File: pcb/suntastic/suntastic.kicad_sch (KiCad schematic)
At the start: 0 parts

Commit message: Rename sheet
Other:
- sheet UVLO with latched output: file uvlo_and latch.kicad_sch -> uvlo_and_latch.kicad_sch
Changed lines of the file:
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@@
       (effects (font (size 1.27 1.27)) (justify left bottom))
     )
-    (property "Sheetfile" "uvlo_and latch.kicad_sch" (at 167.64 65.3546 0) (show_name)
+    (property "Sheetfile" "uvlo_and_latch.kicad_sch" (at 167.64 65.3546 0) (show_name)
       (effects (font (size 1.27 1.27)) (justify left top))
     )

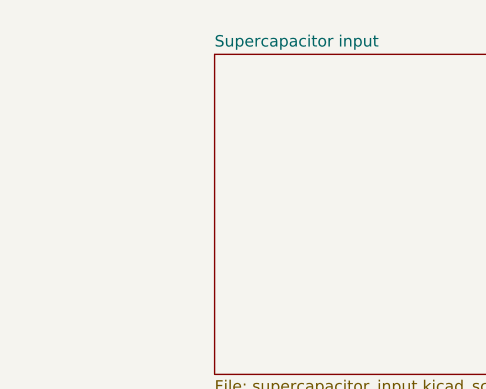
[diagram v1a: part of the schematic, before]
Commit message: Add load switch and RAK connector
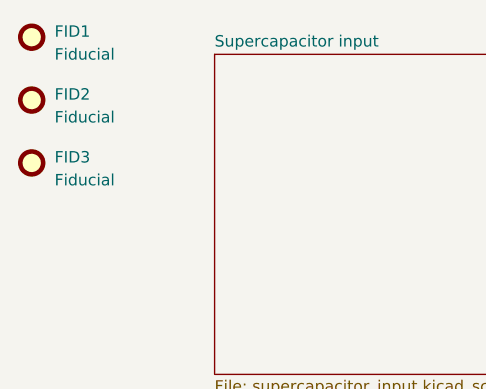
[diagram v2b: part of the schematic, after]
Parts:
- added FID1, FID2, FID3: Fiducial, Fiducial:Fiducial_1mm_Mask3mm, symbol Mechanical:Fiducial
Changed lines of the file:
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@@
     (comment 1 "An ultra low-power management board for meshtastic solar repeater devices.  ")
+  )
+  (symbol (lib_id "Mechanical:Fiducial") (at 24.13 41.275 0) (unit 1)
+    (in_bom yes) (on_board yes) (dnp no) (fields_autoplaced)
+    (property "Reference" "FID3" (at 26.67 40.64 0)
+      (effects (font (size 1.27 1.27)) (justify left))
+    )
+    (property "Value" "Fiducial" (at 26.67 43.18 0)
+      (effects (font (size 1.27 1.27)) (justify left))
+    )
+    (property "Footprint" "Fiducial:Fiducial_1mm_Mask3mm" (at 24.13 41.275 0)
+      (effects (font (size 1.27 1.27)) hide)
+    )
+    (property "Datasheet" "~" (at 24.13 41.275 0)
+      (effects (font (size 1.27 1.27)) hide)
+    )
+    (instances
+      (project "suntastic"
+        (path "/4d5a6178-89d6-4824-ac30-5dee40aabff2"
+          (reference "FID3") (unit 1)
+        )
+      )
+    )
+  )
+  (symbol (lib_id "Mechanical:Fiducial") (at 24.13 27.305 0) (unit 1)
+    (in_bom yes) (on_board yes) (dnp no) (fields_autoplaced)
+    (property "Reference" "FID1" (at 26.67 26.67 0)
+      (effects (font (size 1.27 1.27)) (justify left))
+    )
+    (property "Value" "Fiducial" (at 26.67 29.21 0)
+      (effects (font (size 1.27 1.27)) (justify left))
+    )
+    (property "Footprint" "Fiducial:Fiducial_1mm_Mask3mm" (at 24.13 27.305 0)
+      (effects (font (size 1.27 1.27)) hide)
+    )
+    (property "Datasheet" "~" (at 24.13 27.305 0)
+      (effects (font (size 1.27 1.27)) hide)
+    )
+    (instances
+      (project "suntastic"
+        (path "/4d5a6178-89d6-4824-ac30-5dee40aabff2"
+          (reference "FID1") (unit 1)
+        )
+      )
+    )
+  )
+  (symbol (lib_id "Mechanical:Fiducial") (at 24.13 34.29 0) (unit 1)
+    (in_bom yes) (on_board yes) (dnp no) (fields_autoplaced)
+    (property "Reference" "FID2" (at 26.67 33.655 0)
+      (effects (font (size 1.27 1.27)) (justify left))
+    )
+    (property "Value" "Fiducial" (at 26.67 36.195 0)
+      (effects (font (size 1.27 1.27)) (justify left))
+    )
+    (property "Footprint" "Fiducial:Fiducial_1mm_Mask3mm" (at 24.13 34.29 0)
+      (effects (font (size 1.27 1.27)) hide)
+    )
+    (property "Datasheet" "~" (at 24.13 34.29 0)
+      (effects (font (size 1.27 1.27)) hide)
+    )
+    (instances
+      (project "suntastic"
+        (path "/4d5a6178-89d6-4824-ac30-5dee40aabff2"
+          (reference "FID2") (unit 1)
+        )
+      )
+    )
   )
   (sheet (at 24.13 97.79) (size 74.93 30.48) (fields_autoplaced)

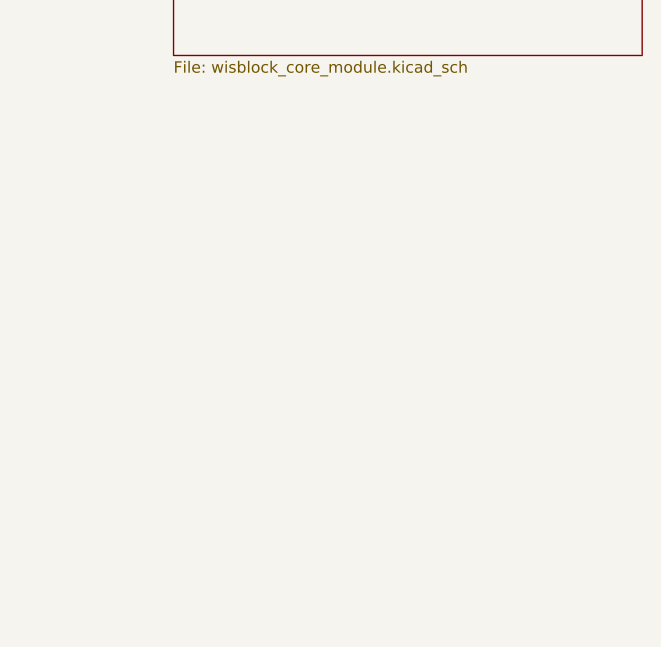
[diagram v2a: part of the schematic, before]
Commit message: Add more doccstrings
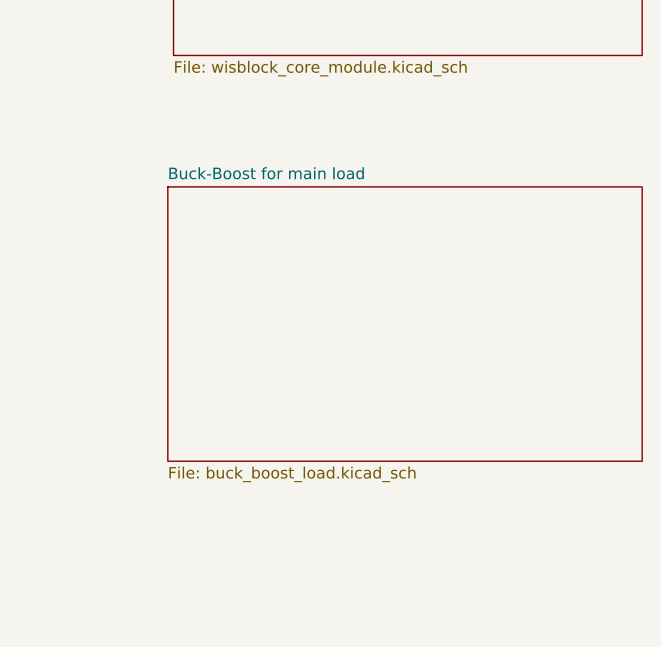
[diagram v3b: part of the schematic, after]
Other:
- added sheet Buck-Boost for main load (buck_boost_load.kicad_sch)
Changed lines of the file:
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@@
+    )
+  )
+  (sheet (at 229.235 127.635) (size 52.705 30.48) (fields_autoplaced)
+    (stroke (width 0.1524) (type solid))
+    (fill (color 0 0 0 0.0000))
+    (property "Sheetname" "Buck-Boost for main load" (at 229.235 126.9234 0)
+      (effects (font (size 1.27 1.27)) (justify left bottom))
+    )
+    (property "Sheetfile" "buck_boost_load.kicad_sch" (at 229.235 158.6996 0)
+      (effects (font (size 1.27 1.27)) (justify left top))
+    )
+    (instances
+      (project "suntastic"
+        (path "/4d5a6178-89d6-4824-ac30-5dee40aabff2" (page "9"))
+      )
     )
   )

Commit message: add wdt
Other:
- added sheet Watchdog timer (watch_dog_timer.kicad_sch)
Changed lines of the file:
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@@
     )
   )
-  (sheet (at 24.13 97.79) (size 74.93 30.48) (fields_autoplaced)
+  (sheet (at 44.45 73.66) (size 48.895 30.48) (fields_autoplaced)
     (stroke (width 0.1524) (type solid))
     (fill (color 0 0 0 0.0000))
-    (property "Sheetname" "MPPT charger" (at 24.13 97.0784 0)
+    (property "Sheetname" "MPPT charger" (at 44.45 72.9484 0)
       (effects (font (size 1.27 1.27)) (justify left bottom))
     )
-    (property "Sheetfile" "mppt_charger.kicad_sch" (at 24.13 128.8546 0)
+    (property "Sheetfile" "mppt_charger.kicad_sch" (at 44.45 104.7246 0)
       (effects (font (size 1.27 1.27)) (justify left top))
     )
@@
     )
   )
-  (sheet (at 167.64 29.21) (size 52.07 35.56) (fields_autoplaced)
+  (sheet (at 167.64 29.21) (size 50.165 35.56) (fields_autoplaced)
     (stroke (width 0.1524) (type solid))
     (fill (color 0 0 0 0.0000))
@@
     )
   )
-  (sheet (at 44.45 29.21) (size 49.53 35.56) (fields_autoplaced)
+  (sheet (at 44.45 29.21) (size 48.895 33.02) (fields_autoplaced)
     (stroke (width 0.1524) (type solid))
     (fill (color 0 0 0 0.0000))
@@
       (effects (font (size 1.27 1.27)) (justify left bottom))
     )
-    (property "Sheetfile" "supercapacitor_input.kicad_sch" (at 44.45 65.3546 0)
+    (property "Sheetfile" "supercapacitor_input.kicad_sch" (at 44.45 62.8146 0)
       (effects (font (size 1.27 1.27)) (justify left top))
     )
@@
     )
   )
-  (sheet (at 25.4 147.32) (size 76.2 27.94) (fields_autoplaced)
+  (sheet (at 167.64 77.47) (size 50.165 35.56) (fields_autoplaced)
     (stroke (width 0.1524) (type solid))
     (fill (color 0 0 0 0.0000))
-    (property "Sheetname" "5W Solar panel input" (at 25.4 146.6084 0)
+    (property "Sheetname" "Watchdog timer" (at 167.64 76.7584 0)
       (effects (font (size 1.27 1.27)) (justify left bottom))
     )
-    (property "Sheetfile" "solar_panel_input.kicad_sch" (at 25.4 175.8446 0)
+    (property "Sheetfile" "watch_dog_timer.kicad_sch" (at 167.64 113.6146 0)
       (effects (font (size 1.27 1.27)) (justify left top))
     )
+    (instances
+      (project "suntastic"
+        (path "/4d5a6178-89d6-4824-ac30-5dee40aabff2" (page "10"))
+      )
+    )
+  )
+  (sheet (at 44.45 118.11) (size 48.895 28.575) (fields_autoplaced)
+    (stroke (width 0.1524) (type solid))
+    (fill (color 0 0 0 0.0000))
+    (property "Sheetname" "5W Solar panel input" (at 44.45 117.3984 0)
+      (effects (font (size 1.27 1.27)) (justify left bottom))
+    )
+    (property "Sheetfile" "solar_panel_input.kicad_sch" (at 44.45 147.2696 0)
+      (effects (font (size 1.27 1.27)) (justify left top))
+    )

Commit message: Rework watchdog
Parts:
- added H1, H2, H3, H4: MountingHole, MountingHole:MountingHole_3mm_Pad, symbol Mechanical:MountingHole
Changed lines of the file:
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@@
+    )
+  )
+  (symbol (lib_id "Mechanical:MountingHole") (at 17.272 65.786 0) (unit 1)
+    (in_bom yes) (on_board yes) (dnp no) (fields_autoplaced)
+    (property "Reference" "H3" (at 20.32 65.151 0)
+      (effects (font (size 1.27 1.27)) (justify left))
+    )
+    (property "Value" "MountingHole" (at 20.32 67.691 0)
+      (effects (font (size 1.27 1.27)) (justify left))
+    )
+    (property "Footprint" "MountingHole:MountingHole_3mm_Pad" (at 17.272 65.786 0)
+      (effects (font (size 1.27 1.27)) hide)
+    )
+    (property "Datasheet" "~" (at 17.272 65.786 0)
+      (effects (font (size 1.27 1.27)) hide)
+    )
+    (instances
+      (project "suntastic"
+        (path "/4d5a6178-89d6-4824-ac30-5dee40aabff2"
+          (reference "H3") (unit 1)
+        )
+      )
     )
   )
@@
         )
       )
+    )
+  )
+  (symbol (lib_id "Mechanical:MountingHole") (at 17.272 71.628 0) (unit 1)
+    (in_bom yes) (on_board yes) (dnp no) (fields_autoplaced)
+    (property "Reference" "H4" (at 20.32 70.993 0)
+      (effects (font (size 1.27 1.27)) (justify left))
+    )
+    (property "Value" "MountingHole" (at 20.32 73.533 0)
+      (effects (font (size 1.27 1.27)) (justify left))
+    )
+    (property "Footprint" "MountingHole:MountingHole_3mm_Pad" (at 17.272 71.628 0)
+      (effects (font (size 1.27 1.27)) hide)
+    )
+    (property "Datasheet" "~" (at 17.272 71.628 0)
+      (effects (font (size 1.27 1.27)) hide)
+    )
+    (instances
+      (project "suntastic"
+        (path "/4d5a6178-89d6-4824-ac30-5dee40aabff2"
+          (reference "H4") (unit 1)
+        )
+      )
+    )
+  )
+  (symbol (lib_id "Mechanical:MountingHole") (at 17.272 59.69 0) (unit 1)
+    (in_bom yes) (on_board yes) (dnp no) (fields_autoplaced)
+    (property "Reference" "H2" (at 20.32 59.055 0)
+      (effects (font (size 1.27 1.27)) (justify left))
+    )
+    (property "Value" "MountingHole" (at 20.32 61.595 0)
+      (effects (font (size 1.27 1.27)) (justify left))
+    )
+    (property "Footprint" "MountingHole:MountingHole_3mm_Pad" (at 17.272 59.69 0)
+      (effects (font (size 1.27 1.27)) hide)
+    )
+    (property "Datasheet" "~" (at 17.272 59.69 0)
+      (effects (font (size 1.27 1.27)) hide)
+    )
+    (instances
+      (project "suntastic"
+        (path "/4d5a6178-89d6-4824-ac30-5dee40aabff2"
+          (reference "H2") (unit 1)
+        )
+      )
+    )
+  )
+  (symbol (lib_id "Mechanical:MountingHole") (at 17.272 53.594 0) (unit 1)
+    (in_bom yes) (on_board yes) (dnp no) (fields_autoplaced)
+    (property "Reference" "H1" (at 20.32 52.959 0)
+      (effects (font (size 1.27 1.27)) (justify left))
+    )
+    (property "Value" "MountingHole" (at 20.32 55.499 0)
+      (effects (font (size 1.27 1.27)) (justify left))
+    )
+    (property "Footprint" "MountingHole:MountingHole_3mm_Pad" (at 17.272 53.594 0)
+      (effects (font (size 1.27 1.27)) hide)
+    )
+    (property "Datasheet" "~" (at 17.272 53.594 0)
+      (effects (font (size 1.27 1.27)) hide)
+    )
+    (instances
+      (project "suntastic"
+        (path "/4d5a6178-89d6-4824-ac30-5dee40aabff2"
+          (reference "H1") (unit 1)
+        )
+      )
